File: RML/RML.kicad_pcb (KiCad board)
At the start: 4 copper layers, 55.8 x 30.6 mm, 23 parts, among them Q1 NMOS, U1 74AHC1G02, U102 641964-1, U103 641964-1, U104 LM555xM, U2 LM7805_TO220, U3 SFH617A-1

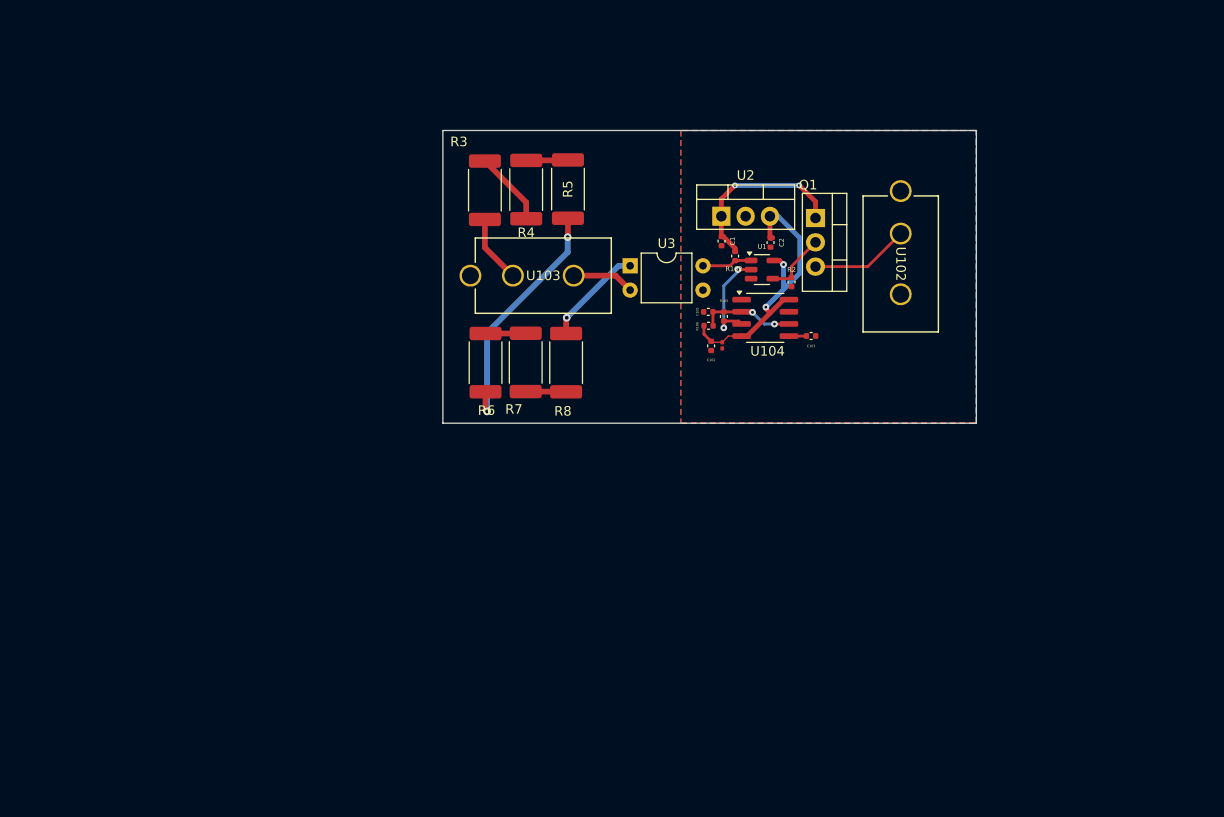
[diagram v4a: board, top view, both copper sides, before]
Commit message: Added changes to RML and re-routed to fit on 1 layer
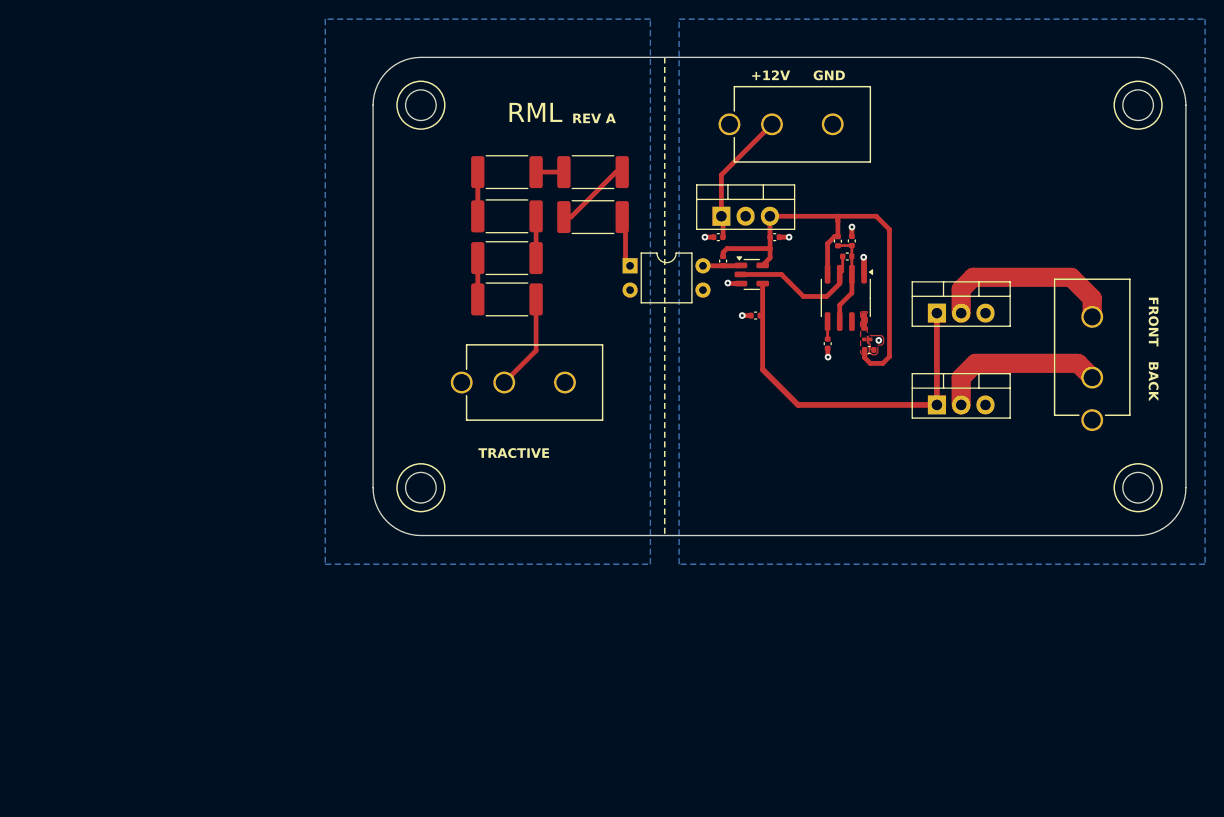
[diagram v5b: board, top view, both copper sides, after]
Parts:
- removed Q1: NMOS, Package_TO_SOT_THT:TO-220-3_Vertical
- added H101: MountingHole, MountingHole:MountingHole_3.2mm_M3, F.Cu at (135.0, 80.0)
- added H102: MountingHole, MountingHole:MountingHole_3.2mm_M3, F.Cu at (60.0, 80.0)
- added H103: MountingHole, MountingHole:MountingHole_3.2mm_M3, F.Cu at (135.0, 40.0)
- added H104: MountingHole, MountingHole:MountingHole_3.2mm_M3, F.Cu at (60.0, 40.0)
- added Q101: Q_NMOS_Depletion_GDS, Package_TO_SOT_THT:TO-220-3_Vertical, F.Cu at (114.0, 71.3)
- added Q102: Q_NMOS_Depletion_GDS, Package_TO_SOT_THT:TO-220-3_Vertical, F.Cu at (114.0, 61.7)
- added U105: 641964-1, CONNECTOR:641964-1_TYC, F.Cu at (96.7, 42.0)
- moved U102 25.1 mm to (130.2, 68.5), turned to 90 degrees
- moved R7 21.1 mm to (78.0, 47.0), turned to 180 degrees
- moved R6 20.0 mm to (69.0, 47.0), turned to 180 degrees
- moved C105 16.7 mm to (105.1, 54.2), turned to -90 degrees
- moved C102 16.5 mm to (106.9, 65.6), turned to 0 degrees
- moved R106 16.2 mm to (103.6, 54.2), turned to 90 degrees
- moved R8 15.5 mm to (78.0, 51.7), turned to 180 degrees
- moved C101 15.2 mm to (106.7, 64.5), turned to 0 degrees
- moved R105 14.3 mm to (104.6, 55.8), turned to 0 degrees
- moved R3 11.6 mm to (69.0, 60.3), turned to 0 degrees
- moved U103 11.2 mm to (68.7, 69.0)
- moved U104 8.68 mm to (104.4, 60.2), turned to -90 degrees
- moved R4 7.44 mm to (69.0, 56.0), turned to 180 degrees
- moved R5 6.99 mm to (69.0, 51.6), turned to 0 degrees
- moved R2 5.14 mm to (95.0, 62.0), turned to 0 degrees
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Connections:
- net Net-(Q1-G) renamed /DRIVE
- R102 pad 1: +12V -> +5V
- U102 pad 2: GND -> Net-(Q102-D)
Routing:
- net /DRIVE: track 6.72 -> 38.3 mm
- net Net-(R5-Pad1): track 26.1 -> 4.62 mm, vias 2 -> 0
- net Net-(Q102-D): track 0.00 -> 19.6 mm
- net +5V: track 32.0 -> 50.2 mm, vias 2 -> 0
- net GND: track 0.00 -> 7.95 mm, vias 0 -> 8
- net Net-(Q101-D): track 10.7 -> 17.8 mm
- net GNDPWR: track 6.53 -> 0.00 mm
- net 12.5 mA: track 10.9 -> 5.44 mm, vias 1 -> 0
- net +12V: track 19.1 -> 14.1 mm, vias 2 -> 0
- net CLOCK: track 10.8 -> 14.8 mm, vias 2 -> 0
- net Net-(R7-Pad1): track 4.23 -> 8.05 mm
- net Net-(R3-Pad1): track 7.82 -> 4.32 mm
- net 352.8V: track 7.10 -> 10.1 mm
- net Net-(R6-Pad1): track 4.21 -> 2.90 mm
- net Net-(R102-Pad2): track 5.26 -> 3.98 mm
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- added copper zone on F.Cu, net +5V
- added copper zone on B.Cu, net GNDPWR
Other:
- board size 55.8 x 30.6 mm -> 85 x 50 mm
- board text added: "+12V"
- board text added: "BACK"
- board text added: "FRONT"
- board text added: "GND"
- board text added: "REV A"
- board text added: "RML"
- board text added: "TRACTIVE"

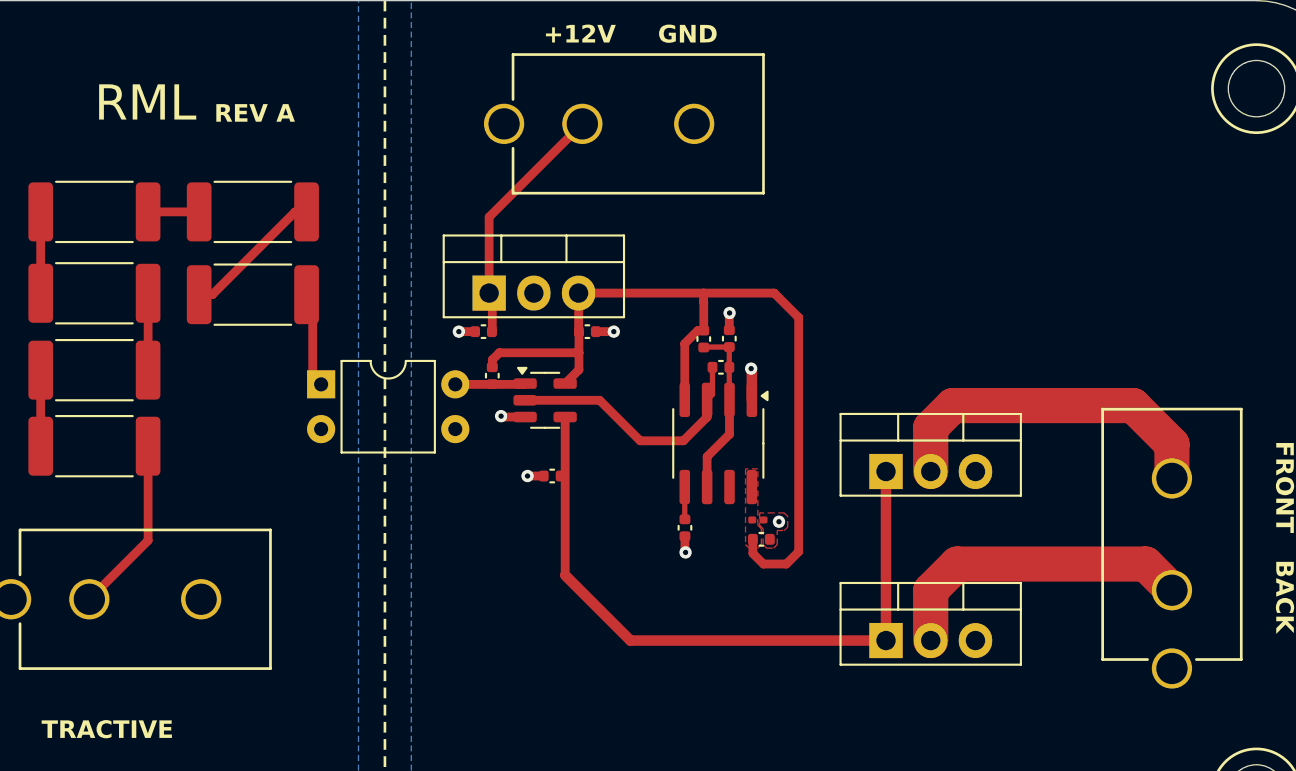
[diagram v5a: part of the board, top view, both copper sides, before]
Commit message: Updated RML BOM
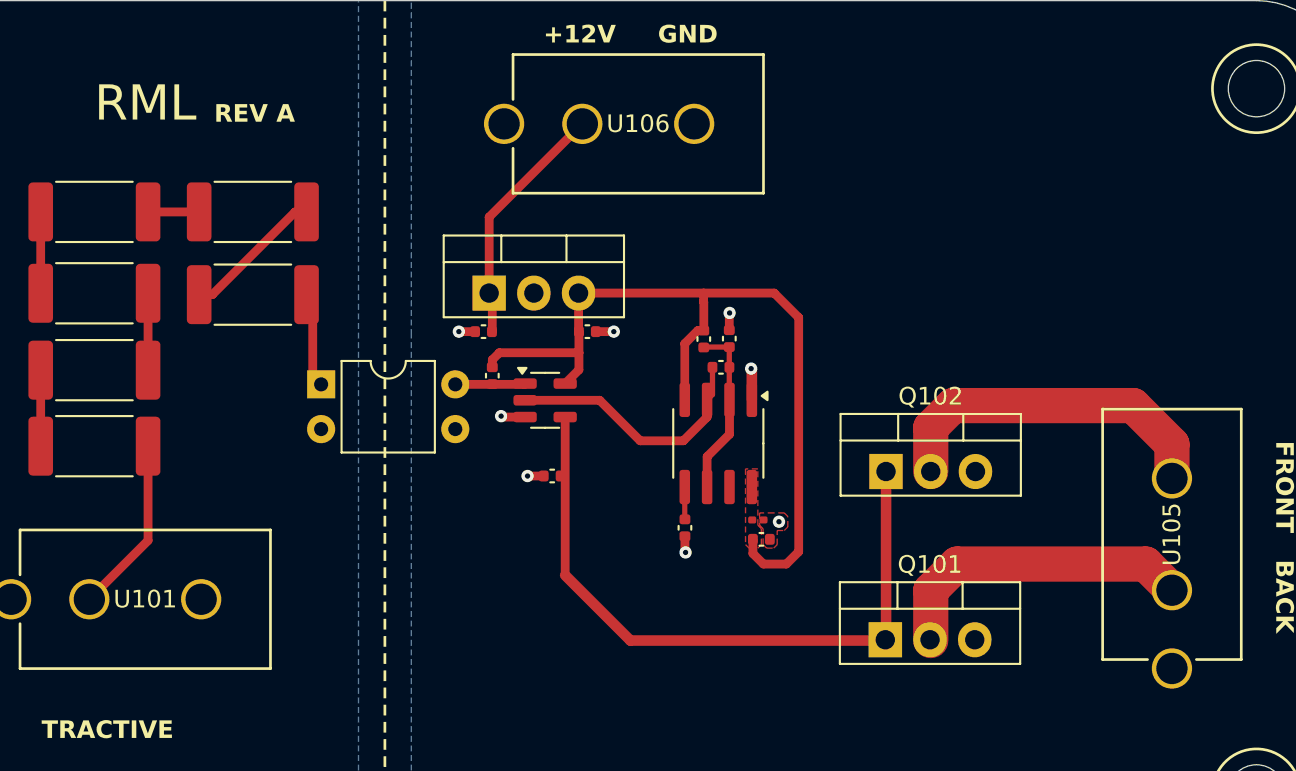
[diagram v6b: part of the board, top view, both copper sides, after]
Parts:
- C103: value .01u -> 0.01u
- C105: renamed from C1; value 0.33uF -> 0.33u
- C106: renamed from C2; value 0.01uF -> 0.01u
- Q101, Q102: value Q_NMOS_Depletion_GDS -> Q_NMOS_GDS
- moved Q101 0.06 mm to (113.9, 71.3)
- renumbered C105 to C104, H103 to H102, H102 to H103, R3 to R101, R4 to R102, R5 to R103, R6 to R104, R7 to R106, R106 to R107, R8 to R108, R102 to R109, R2 to R110, U103 to U101, U104 to U102, U3 to U103, U1 to U104, U102 to U105, U105 to U106, U2 to U107

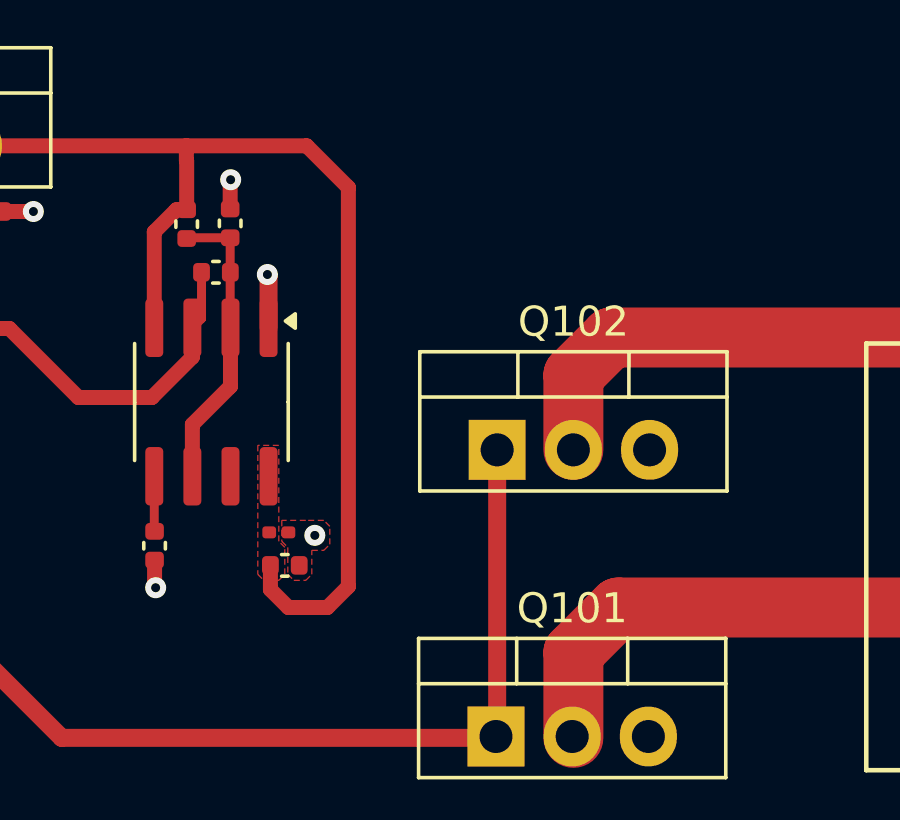
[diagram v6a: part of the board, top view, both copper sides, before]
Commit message: Fixed RML footprint issues
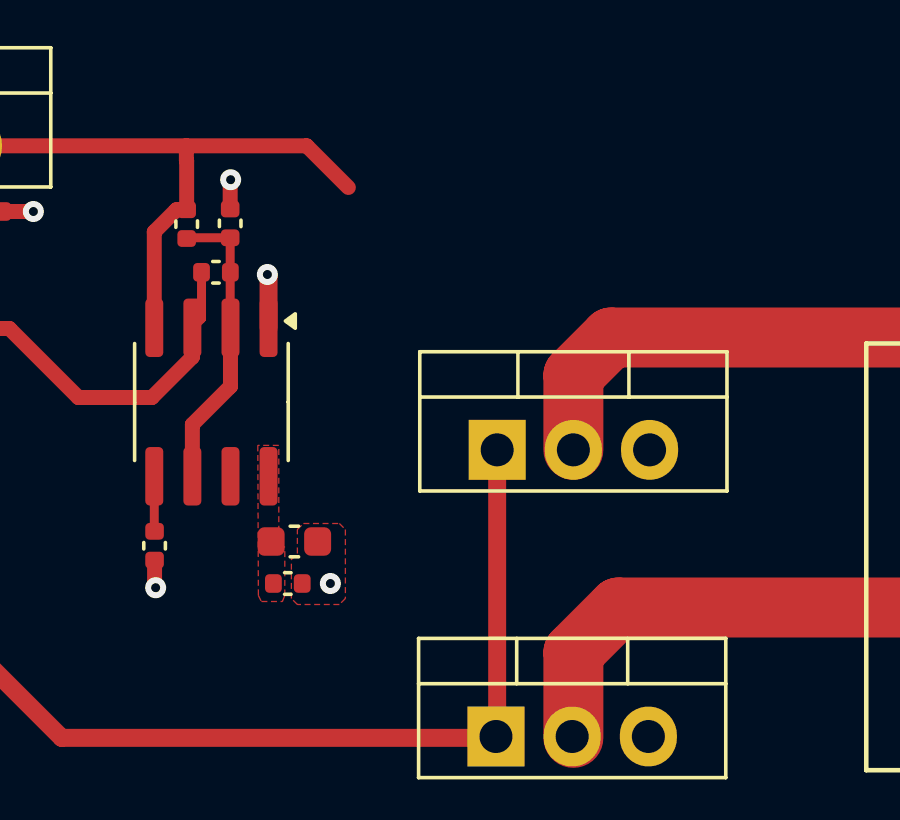
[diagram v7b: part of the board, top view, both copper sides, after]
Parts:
- C101: footprint Capacitor_SMD:C_0201_0603Metric -> Capacitor_SMD:C_0603_1608Metric
- moved C102 0.61 mm to (107.0, 66.2)
- moved C101 0.60 mm to (107.2, 64.8)
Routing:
- net +5V: track 50.2 -> 32.9 mm
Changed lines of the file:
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@@
 			(at 2.54 -4.27 0)
 			(layer "F.SilkS")
+			(hide yes)
 			(effects
 				(font
@@
 	(footprint "Capacitor_SMD:C_0402_1005Metric"
 		(layer "F.Cu")
-		(at 106.880992 65.595485)
+		(at 106.980992 66.2)
 		(descr "Capacitor SMD 0402 (1005 Metric), square (rectangular) end terminal, IPC_7351 nominal, (Body size source: IPC-SM-782 page 76, https://www.pcb-3d.com/wordpress/wp-content/uploads/ipc-sm-782a_amendment_1_and_2.pdf), generated with kicad-footprint-generator")
 		(tags "capacitor")
@@
 		)
 	)
-	(footprint "Capacitor_SMD:C_0201_0603Metric"
+	(footprint "Capacitor_SMD:C_0603_1608Metric"
 		(layer "F.Cu")
-		(at 106.680992 64.495485)
-		(descr "Capacitor SMD 0201 (0603 Metric), square (rectangular) end terminal, IPC_7351 nominal, (Body size source: https://www.vishay.com/docs/20052/crcw0201e3.pdf), generated with kicad-footprint-generator")
+		(at 107.2 64.8)
+		(descr "Capacitor SMD 0603 (1608 Metric), square (rectangular) end terminal, IPC_7351 nominal, (Body size source: IPC-SM-782 page 76, https://www.pcb-3d.com/wordpress/wp-content/uploads/ipc-sm-782a_amendment_1_and_2.pdf), generated with kicad-footprint-generator")
 		(tags "capacitor")
 		(property "Reference" "C101"
-			(at 0.88 -2.425 0)
+			(at 0 -1.43 0)
 			(layer "F.SilkS")
 			(hide yes)
@@
 		)
 		(property "Value" "1u"
-			(at 0.895 0 90)
+			(at 0 1.43 0)
 			(layer "F.Fab")
 			(effects
 				(font
-					(size 0.25 0.25)
-					(thickness 0.03125)
+					(size 1 1)
+					(thickness 0.15)
 				)
 			)
@@
 		(attr smd)
 		(fp_line
-			(start -0.7 -0.35)
-			(end 0.7 -0.35)
+			(start -0.14058 -0.51)
+			(end 0.14058 -0.51)
+			(stroke
+				(width 0.12)
+				(type solid)
+			)
+			(layer "F.SilkS")
+		)
+		(fp_line
+			(start -0.14058 0.51)
+			(end 0.14058 0.51)
+			(stroke
+				(width 0.12)
+				(type solid)
+			)
+			(layer "F.SilkS")
+		)
+		(fp_line
+			(start -1.48 -0.73)
+			(end 1.48 -0.73)
 			(stroke
 				(width 0.05)
@@
 		)
 		(fp_line
-			(start -0.7 0.35)
-			(end -0.7 -0.35)
+			(start -1.48 0.73)
+			(end -1.48 -0.73)
 			(stroke
 				(width 0.05)
@@
 		)
 		(fp_line
-			(start 0.7 -0.35)
-			(end 0.7 0.35)
+			(start 1.48 -0.73)
+			(end 1.48 0.73)
 			(stroke
 				(width 0.05)
@@
 		)
 		(fp_line
-			(start 0.7 0.35)
-			(end -0.7 0.35)
+			(start 1.48 0.73)
+			(end -1.48 0.73)
 			(stroke
 				(width 0.05)
@@
 		)
 		(fp_line
-			(start -0.3 -0.15)
-			(end 0.3 -0.15)
+			(start -0.8 -0.4)
+			(end 0.8 -0.4)
 			(stroke
 				(width 0.1)
@@
 		)
 		(fp_line
-			(start -0.3 0.15)
-			(end -0.3 -0.15)
+			(start -0.8 0.4)
+			(end -0.8 -0.4)
 			(stroke
 				(width 0.1)
@@
 		)
 		(fp_line
-			(start 0.3 -0.15)
-			(end 0.3 0.15)
+			(start 0.8 -0.4)
+			(end 0.8 0.4)
 			(stroke
 				(width 0.1)
@@
 		)
 		(fp_line
-			(start 0.3 0.15)
-			(end -0.3 0.15)
+			(start 0.8 0.4)
+			(end -0.8 0.4)
 			(stroke
 				(width 0.1)
@@
 		)
 		(fp_text user "${REFERENCE}"
-			(at 0.02 -0.575 0)
+			(at 0 0 0)
 			(layer "F.Fab")
 			(effects
 				(font
-					(size 0.25 0.25)
-					(thickness 0.04)
+					(size 0.4 0.4)
+					(thickness 0.06)
 				)
 			)
 		)
-		(pad "" smd roundrect
-			(at -0.345 0)
-			(size 0.318 0.36)
-			(layers "F.Paste")
-			(roundrect_rratio 0.25)
-		)
-		(pad "" smd roundrect
-			(at 0.345 0)
-			(size 0.318 0.36)
-			(layers "F.Paste")
-			(roundrect_rratio 0.25)
-		)
 		(pad "1" smd roundrect
-			(at -0.32 0)
-			(size 0.46 0.4)
-			(layers "F.Cu" "F.Mask")
+			(at -0.775 0)
+			(size 0.9 0.95)
+			(layers "F.Cu" "F.Mask" "F.Paste")
 			(roundrect_rratio 0.25)
 			(net 4 "+5V")
@@
 		)
 		(pad "2" smd roundrect
-			(at 0.32 0)
-			(size 0.46 0.4)
-			(layers "F.Cu" "F.Mask")
+			(at 0.775 0)
+			(size 0.9 0.95)
+			(layers "F.Cu" "F.Mask" "F.Paste")
 			(roundrect_rratio 0.25)
 			(net 3 "GND")
@@
 		)
 		(embedded_fonts no)
-		(model "${KICAD9_3DMODEL_DIR}/Capacitor_SMD.3dshapes/C_0201_0603Metric.wrl"
+		(model "${KICAD9_3DMODEL_DIR}/Capacitor_SMD.3dshapes/C_0603_1608Metric.wrl"
 			(offset
 				(xyz 0 0 0)
@@
 			(at 2.54 -4.27 0)
 			(layer "F.SilkS")
+			(hide yes)
 			(effects
 				(font
@@
 	)
 	(via
-		(at 107.880992 64.595485)
+		(at 108.4 66.2)
 		(size 0.7)
 		(drill 0.3)
@@
 	)
 	(segment
-		(start 108.3 67)
-		(end 109 66.3)
-		(width 0.5)
-		(layer "F.Cu")
-		(net 4)
-	)
-	(segment
 		(start 96.52 55)
 		(end 96.52 55.9675)
@@
 	)
 	(segment
-		(start 106.400992 65.595485)
-		(end 106.400992 66.400992)
-		(width 0.5)
-		(layer "F.Cu")
-		(net 4)
-	)
-	(segment
 		(start 96.5 53.826)
 		(end 96.56 53.886)
@@
 	)
 	(segment
-		(start 106.400992 66.400992)
-		(end 107 67)
-		(width 0.5)
-		(layer "F.Cu")
-		(net 4)
-	)
-	(segment
 		(start 106.34 62.06676)
 		(end 106.34 62.62586)
@@
 	)
 	(segment
-		(start 107 67)
-		(end 108.3 67)
-		(width 0.5)
-		(layer "F.Cu")
-		(net 4)
-	)
-	(segment
 		(start 103.6 51.611)
 		(end 96.5 51.611)
@@
 	)
 	(segment
-		(start 109 66.3)
-		(end 109 53)
-		(width 0.5)
-		(layer "F.Cu")
-		(net 4)
-	)
-	(segment
 		(start 96.52 55)
 		(end 92 55)
@@
 	)
 	(zone
-		(net 3)
-		(net_name "GND")
+		(net 4)
+		(net_name "+5V")
 		(layer "F.Cu")
 		(hatch edge 0.5)
-		(priority 3)
 		(connect_pads yes
 			(clearance 0)
@@
 		(polygon
 			(pts
-				(xy 106.980992 65.895485) (xy 107.180992 66.095485) (xy 107.580992 66.095485) (xy 107.780992 65.895485)
-				(xy 107.780992 65.095485) (xy 108.180992 65.095485) (xy 108.380992 64.895485) (xy 108.380992 64.295485)
-				(xy 108.180992 64.095485) (xy 107.580992 64.095485) (xy 106.780992 64.095485) (xy 106.780992 64.795485)
-				(xy 106.980992 64.995485)
+				(xy 106.880992 64.995485) (xy 106.680992 64.795485) (xy 106.680992 61.595485) (xy 105.980992 61.595485)
+				(xy 106 66.6) (xy 106.1 66.8) (xy 106.8 66.8) (xy 106.880992 66.6)
 			)
 		)
 	)
 	(zone
-		(net 4)
-		(net_name "+5V")
+		(net 3)
+		(net_name "GND")
 		(layer "F.Cu")
 		(hatch edge 0.5)
+		(priority 3)
 		(connect_pads yes
 			(clearance 0)
@@
 		(polygon
 			(pts
-				(xy 106.880992 64.995485) (xy 106.680992 64.795485) (xy 106.680992 61.595485) (xy 105.980992 61.595485)
-				(xy 105.980992 65.895485) (xy 106.180992 66.095485) (xy 106.680992 66.095485) (xy 106.880992 65.895485)
+				(xy 107.3 64.4) (xy 107.5 64.2) (xy 108.7 64.2) (xy 108.9 64.4) (xy 108.9 66.7) (xy 108.7 66.9)
+				(xy 107.3 66.9) (xy 107.1 66.7) (xy 107.1 65.4) (xy 107.3 65.2)
 			)
 		)
